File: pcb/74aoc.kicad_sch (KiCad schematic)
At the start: 0 parts

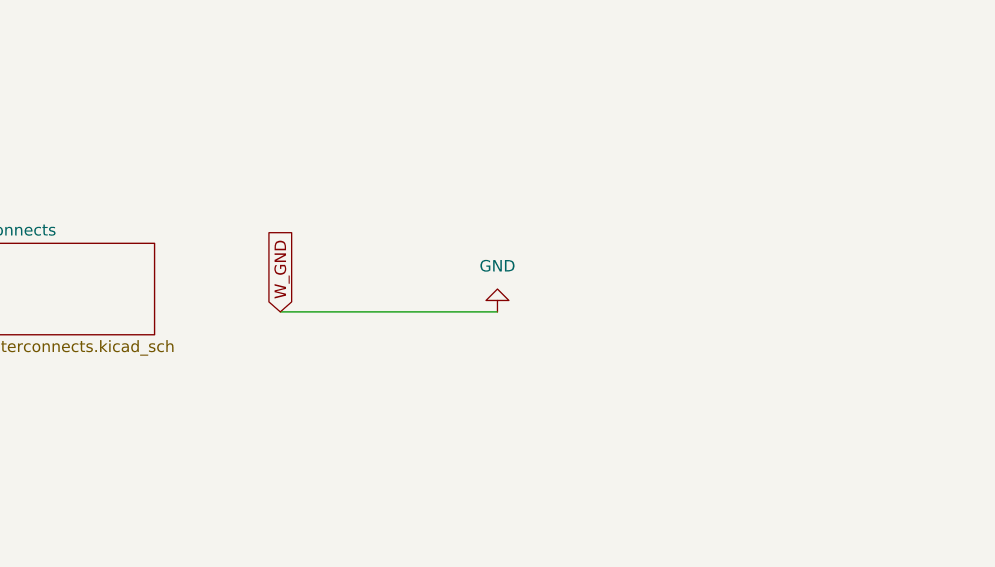
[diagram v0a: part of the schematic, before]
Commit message: Bake everything into the PCB (+ commit the intermediates)
This is mostly for traceability reproducibility reasons.
In practice, the best way to bake a different design would be to branch
off just before this commit
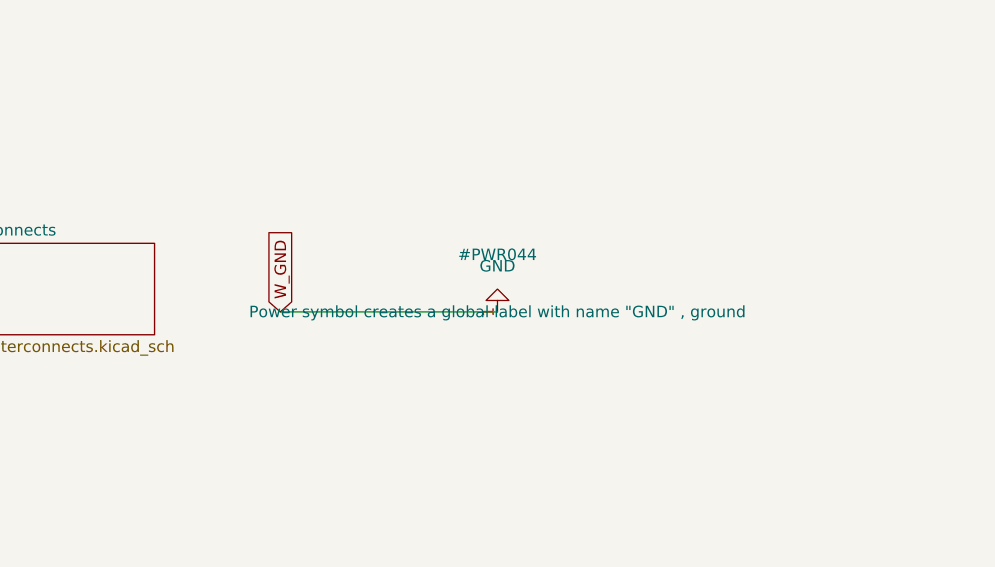
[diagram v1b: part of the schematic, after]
